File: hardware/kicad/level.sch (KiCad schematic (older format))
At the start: 0 parts

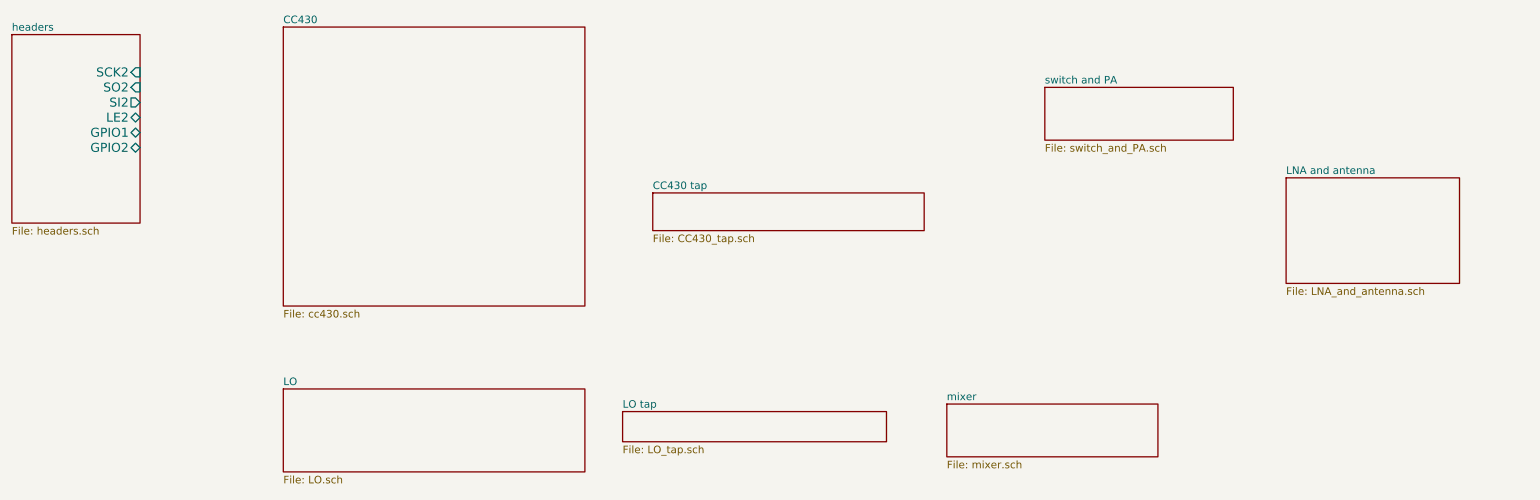
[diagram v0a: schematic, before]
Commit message: Added taps to schematic
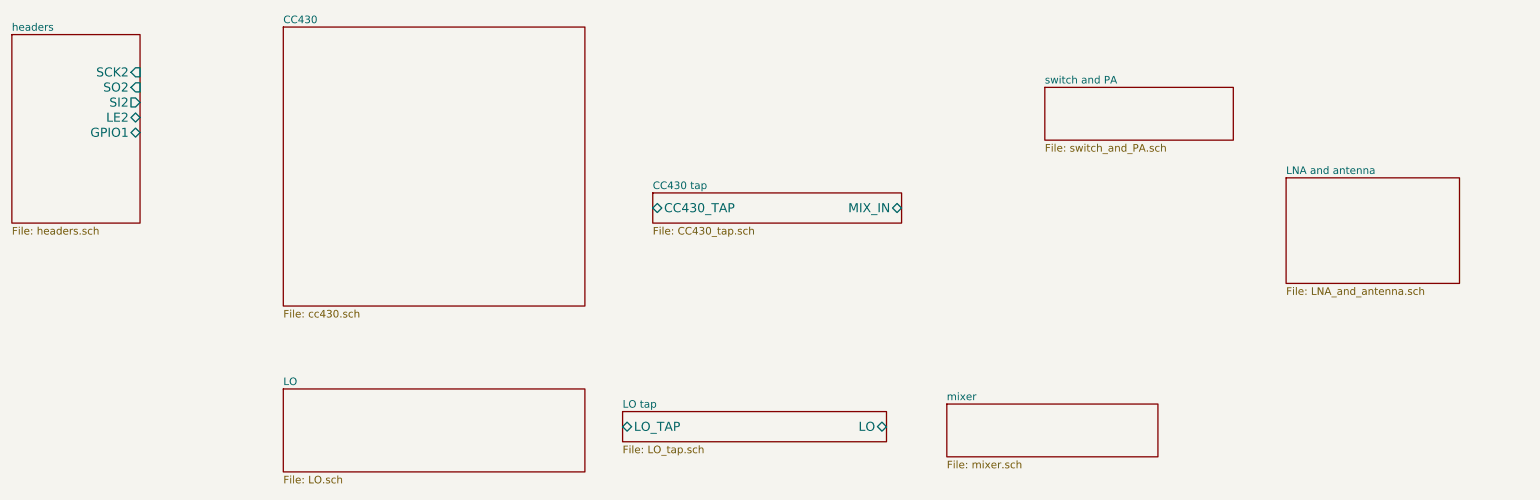
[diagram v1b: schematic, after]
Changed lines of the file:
@@
 LIBS:contrib
 LIBS:valves
+LIBS:level
 LIBS:level-cache
 EELAYER 27 0
@@
 Sheet 1 9
 Title ""
-Date "20 sep 2014"
+Date "26 sep 2014"
 Rev ""
 Comp ""
@@
 F0 "LO tap" 50
 F1 "LO_tap.sch" 50
+F2 "LO" B R 6900 4750 60
+F3 "LO_TAP" B L 5150 4750 60
 $EndSheet
 $Sheet
-S 5350 3200 1800 250
+S 5350 3200 1650 200
 U 541CD79C
 F0 "CC430 tap" 50
 F1 "CC430_tap.sch" 50
+F2 "CC430_TAP" B L 5350 3300 60
+F3 "MIX_IN" B R 7000 3300 60
 $EndSheet
 $Sheet
@@
 F5 "LE2" B R 1950 2700 60
 F6 "GPIO1" B R 1950 2800 60
-F7 "GPIO2" B R 1950 2900 60
 $EndSheet
 $EndSCHEMATC

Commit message: Finished port from Altium to KiCAD
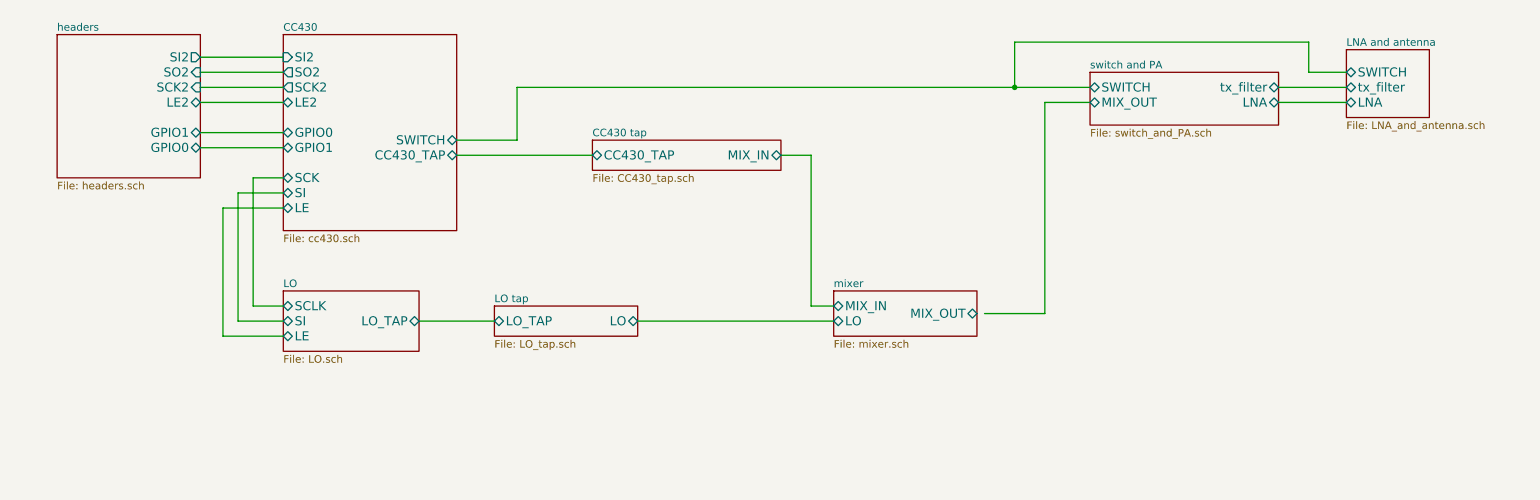
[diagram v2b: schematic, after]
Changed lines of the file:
@@
 Sheet 1 9
 Title ""
-Date "26 sep 2014"
+Date "27 sep 2014"
 Rev ""
 Comp ""
@@
 $EndDescr
 $Sheet
-S 2900 2100 2000 1850
+S 2900 3850 900  400
+U 541CD777
+F0 "LO" 50
+F1 "LO.sch" 50
+F2 "SCLK" B L 2900 3950 60
+F3 "SI" B L 2900 4050 60
+F4 "LE" B L 2900 4150 60
+F5 "LO_TAP" B R 3800 4050 60
+$EndSheet
+$Sheet
+S 4300 3950 950  200
+U 541CD787
+F0 "LO tap" 50
+F1 "LO_tap.sch" 50
+F2 "LO" B R 5250 4050 60
+F3 "LO_TAP" B L 4300 4050 60
+$EndSheet
+$Sheet
+S 4950 2850 1250 200
+U 541CD79C
+F0 "CC430 tap" 50
+F1 "CC430_tap.sch" 50
+F2 "CC430_TAP" B L 4950 2950 60
+F3 "MIX_IN" B R 6200 2950 60
+$EndSheet
+$Sheet
+S 6550 3850 950  300
+U 541CD7B4
+F0 "mixer" 50
+F1 "mixer.sch" 50
+F2 "LO" B L 6550 4050 60
+F3 "MIX_IN" B L 6550 3950 60
+F4 "MIX_OUT" B R 7500 4000 60
+$EndSheet
+$Sheet
+S 8250 2400 1250 350
+U 541CD7C5
+F0 "switch and PA" 50
+F1 "switch_and_PA.sch" 50
+F2 "SWITCH" B L 8250 2500 60
+F3 "MIX_OUT" B L 8250 2600 60
+F4 "LNA" B R 9500 2600 60
+F5 "tx_filter" B R 9500 2500 60
+$EndSheet
+$Sheet
+S 9950 2250 550  450
+U 541CD7D7
+F0 "LNA and antenna" 50
+F1 "LNA_and_antenna.sch" 50
+F2 "LNA" B L 9950 2600 60
+F3 "SWITCH" B L 9950 2400 60
+F4 "tx_filter" B L 9950 2500 60
+$EndSheet
+$Sheet
+S 1400 2150 950  950
+U 541CD74E
+F0 "headers" 50
+F1 "headers.sch" 50
+F2 "SCK2" I R 2350 2500 60
+F3 "SO2" I R 2350 2400 60
+F4 "SI2" O R 2350 2300 60
+F5 "LE2" B R 2350 2600 60
+F6 "GPIO1" B R 2350 2800 60
+F7 "GPIO0" B R 2350 2900 60
+$EndSheet
+$Sheet
+S 2900 2150 1150 1300
 U 541CD765
 F0 "CC430" 50
 F1 "cc430.sch" 50
+F2 "SWITCH" B R 4050 2850 60
+F3 "GPIO0" B L 2900 2800 60
+F4 "GPIO1" B L 2900 2900 60
+F5 "SI" B L 2900 3200 60
+F6 "LE2" B L 2900 2600 60
+F7 "SCK" B L 2900 3100 60
+F8 "LE" B L 2900 3300 60
+F9 "CC430_TAP" B R 4050 2950 60
+F10 "SI2" I L 2900 2300 60
+F11 "SCK2" O L 2900 2500 60
+F12 "SO2" O L 2900 2400 60
 $EndSheet
-$Sheet
-S 2900 4500 2000 550
-U 541CD777
-F0 "LO" 50
-F1 "LO.sch" 50
-$EndSheet
-$Sheet
-S 5150 4650 1750 200
-U 541CD787
-F0 "LO tap" 50
-F1 "LO_tap.sch" 50
-F2 "LO" B R 6900 4750 60
-F3 "LO_TAP" B L 5150 4750 60
-$EndSheet
-$Sheet
-S 5350 3200 1650 200
-U 541CD79C
-F0 "CC430 tap" 50
-F1 "CC430_tap.sch" 50
-F2 "CC430_TAP" B L 5350 3300 60
-F3 "MIX_IN" B R 7000 3300 60
-$EndSheet
-$Sheet
-S 7300 4600 1400 350
-U 541CD7B4
-F0 "mixer" 50
-F1 "mixer.sch" 50
-$EndSheet
-$Sheet
-S 7950 2500 1250 350
-U 541CD7C5
-F0 "switch and PA" 50
-F1 "switch_and_PA.sch" 50
-$EndSheet
-$Sheet
-S 9550 3100 1150 700
-U 541CD7D7
-F0 "LNA and antenna" 50
-F1 "LNA_and_antenna.sch" 50
-$EndSheet
-$Sheet
-S 1100 2150 850  1250
-U 541CD74E
-F0 "headers" 50
-F1 "headers.sch" 50
-F2 "SCK2" I R 1950 2400 60
-F3 "SO2" I R 1950 2500 60
-F4 "SI2" O R 1950 2600 60
-F5 "LE2" B R 1950 2700 60
-F6 "GPIO1" B R 1950 2800 60
-$EndSheet
+Wire Wire Line
+	2350 2300 2900 2300
+Wire Wire Line
+	2350 2400 2900 2400
+Wire Wire Line
+	2350 2500 2900 2500
+Wire Wire Line
+	2350 2600 2900 2600
+Wire Wire Line
+	2350 2800 2900 2800
+Wire Wire Line
+	2350 2900 2900 2900
+Wire Wire Line
+	4050 2950 4950 2950
+Wire Wire Line
+	2900 3100 2700 3100
+Wire Wire Line
+	2700 3100 2700 3950
+Wire Wire Line
+	2700 3950 2900 3950
+Wire Wire Line
+	2900 3200 2600 3200
+Wire Wire Line
+	2600 3200 2600 4050
+Wire Wire Line
+	2600 4050 2900 4050
+Wire Wire Line
+	2900 3300 2500 3300
+Wire Wire Line
+	2500 3300 2500 4150
+Wire Wire Line
+	2500 4150 2900 4150
+Wire Wire Line
+	3800 4050 4300 4050
+Wire Wire Line
+	5250 4050 6550 4050
+Wire Wire Line
+	6200 2950 6400 2950
+Wire Wire Line
+	6400 2950 6400 3950
+Wire Wire Line
+	6400 3950 6550 3950
+Wire Wire Line
+	8250 2500 4450 2500
+Wire Wire Line
+	4450 2500 4450 2850
+Wire Wire Line
+	4450 2850 4050 2850
+Wire Wire Line
+	7550 4000 7950 4000
+Wire Wire Line
+	7950 4000 7950 2600
+Wire Wire Line
+	7950 2600 8250 2600
+Wire Wire Line
+	9500 2600 9950 2600
+Wire Wire Line
+	9500 2500 9950 2500
+Wire Wire Line
+	9700 2400 9950 2400
+Wire Wire Line
+	9700 2400 9700 2200
+Wire Wire Line
+	9700 2200 7750 2200
+Wire Wire Line
+	7750 2200 7750 2500
+Connection ~ 7750 2500
 $EndSCHEMATC
